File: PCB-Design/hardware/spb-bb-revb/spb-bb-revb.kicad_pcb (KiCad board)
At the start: 4 copper layers, 89.5 x 80 mm, 236 parts, among them J1 DC+, J10 U.FL L2, J11 U.FL D2, J12 DC+, J13 DC-, J14 V_ISO,HS in: 1 +, 2 -, J15 V_ISO,LS in: 1 +, 2 -, J16 CTRL2: 1 12V 2 GND 3 PWM_H 4 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, J17 FAN 12V: 1 +12V, 2 GND, J18 U.FL H3, J19 U.FL L3, J2 DC-, J20 U.FL D3, J21 U.FL H4, J22 U.FL L4, J23 U.FL D4, J24 AC, J25 AC, J26 AC, J27 AC, J28 1:NTC 2:DC- (LS domain!), J3 V_ISO,HS in: 1 +, 2 -, J4 V_ISO,LS in: 1 +, 2 -, J5 CTRL1: 1 12V 2 GND 3 PWM_H 4 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, J6 U.FL H1, J7 U.FL L1, J8 U.FL D1, J9 U.FL H2, Q1 EPC2361, Q2 EPC2361, Q3 EPC2361, Q4 EPC2361, Q5 EPC2361, Q6 EPC2361, Q7 EPC2361, Q8 EPC2361, U1 2EDF7275K, U2 2EDF7275K

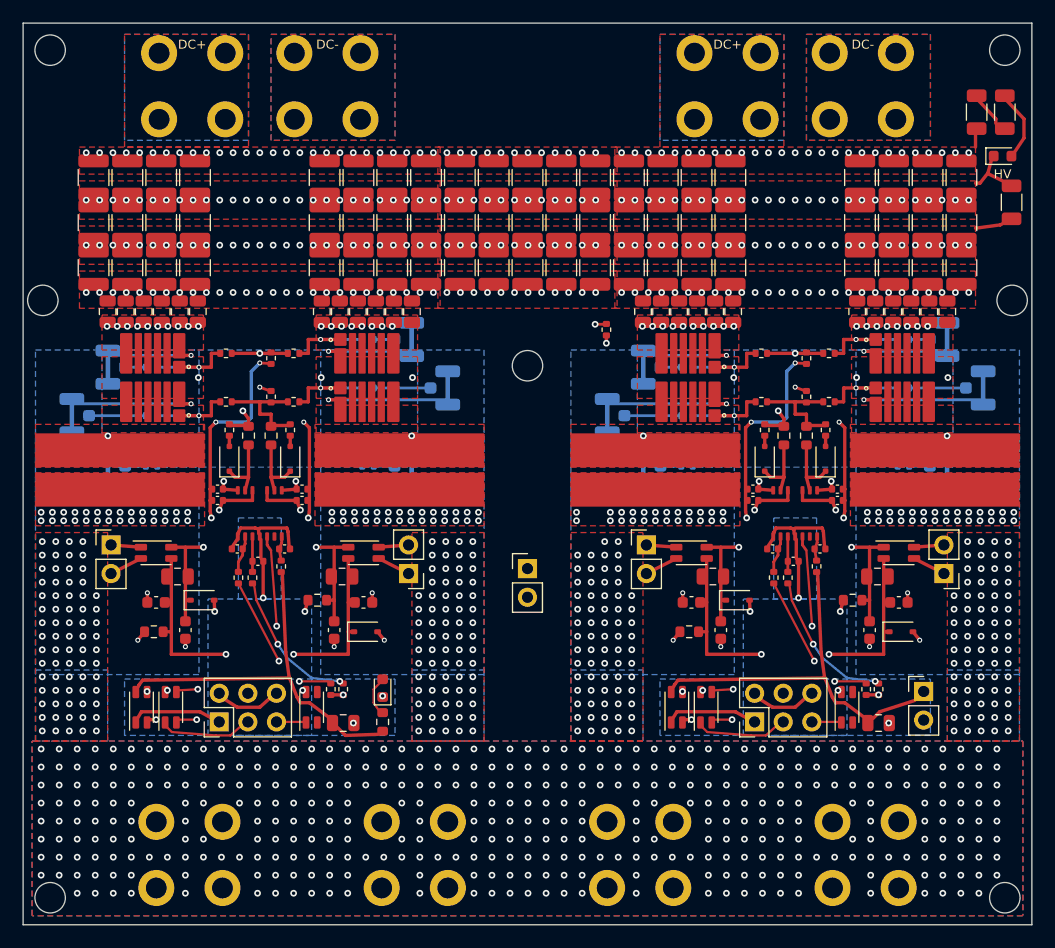
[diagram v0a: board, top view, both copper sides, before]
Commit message: ﻿Rev B as one leg: one DC pair, one AC bolt pad (option B drivers)
- make_kicad_bb_revb.py: one DC+/DC- REDCUBE pair at the centre feeding a laminated
  terminal row (L1/L3 DC+, L2/L4 DC-) over the full width; the four AC terminals replaced
  by one M6 bolt pad (AC_BOLT_M6, 14 mm pad, via rings); two drivers, one star per pair.
  231 parts, DRC 0/0/0, routing 0 failures
- schematic regenerated, check_sch_vs_pcb: 0 problems
- busbar: one DC pair per leg (6 bolt points), DRC clean
- Q3D export/post for the new terminals; leg Q3D setup at 2 % convergence
- deck: step 8 slides for the new layout (Q3D numbers follow)
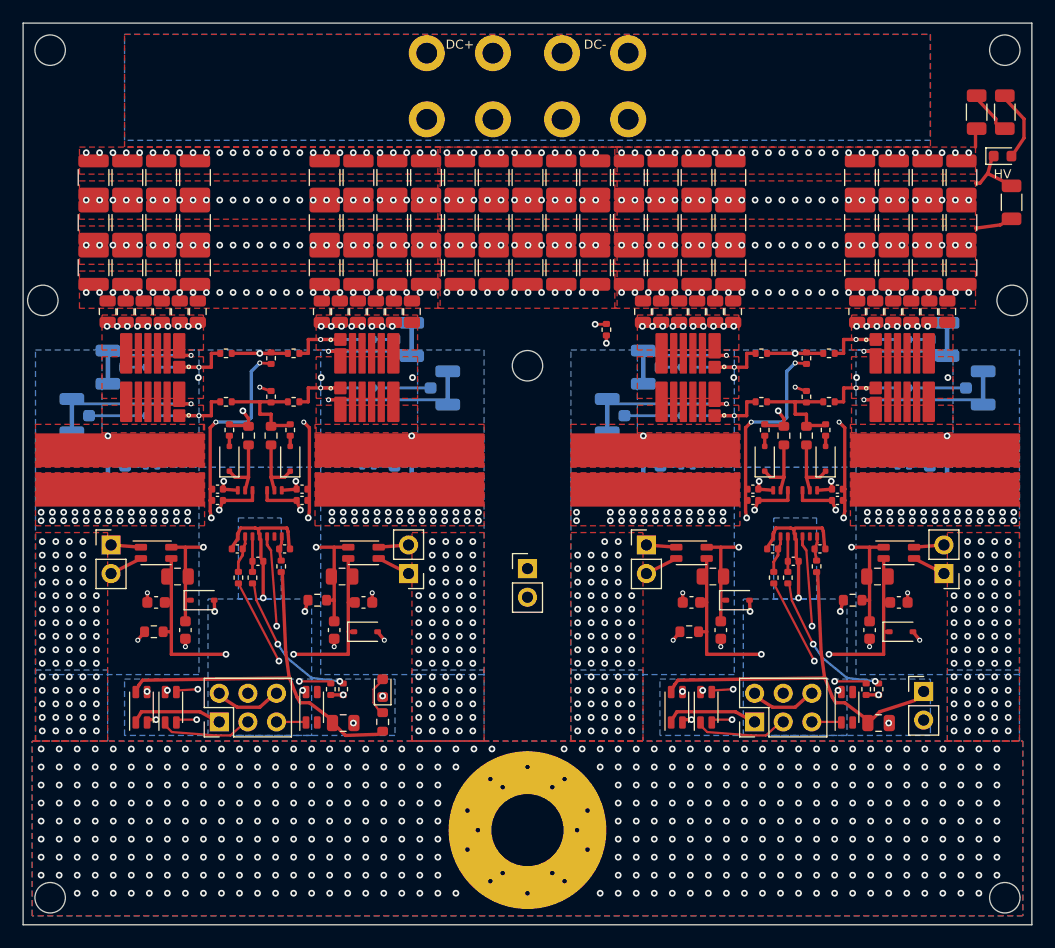
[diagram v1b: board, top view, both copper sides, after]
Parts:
- removed J24, J25, J26, J27: AC, TerminalBlock_Wuerth:Wuerth_REDCUBE-THR_WP-THRBU_74650174_THR
- removed J28: 1:NTC 2:DC- (LS domain!), Connector_PinHeader_2.54mm:PinHeader_1x02_P2.54mm_Vertical
- J12: value DC+ -> V_ISO,HS in: 1 +, 2 -; footprint TerminalBlock_Wuerth:Wuerth_REDCUBE-THR_WP-THRBU_74650174_THR -> Connector_PinHeader_2.54mm:PinHeader_1x02_P2.54mm_Vertical; moved to F.Cu
- J13: value DC- -> V_ISO,LS in: 1 +, 2 -; footprint TerminalBlock_Wuerth:Wuerth_REDCUBE-THR_WP-THRBU_74650174_THR -> Connector_PinHeader_2.54mm:PinHeader_1x02_P2.54mm_Vertical; moved to F.Cu
- J14: value V_ISO,HS in: 1 +, 2 - -> CTRL2: 1 12V 2 GND 3 PWM_H 4 PWM_L 5 DIS 6 GND; footprint Connector_PinHeader_2.54mm:PinHeader_1x02_P2.54mm_Vertical -> Connector_PinHeader_2.54mm:PinHeader_2x03_P2.54mm_Vertical
- J15: value V_ISO,LS in: 1 +, 2 - -> FAN 12V: 1 +12V, 2 GND
- J16: value CTRL2: 1 12V 2 GND 3 PWM_H 4 PWM_L 5 DIS 6 GND -> U.FL H3; footprint Connector_PinHeader_2.54mm:PinHeader_2x03_P2.54mm_Vertical -> spb_fab:U.FL_Hirose_U.FL-R-SMT-1_Vertical; moved to B.Cu
- J17: value FAN 12V: 1 +12V, 2 GND -> U.FL L3; footprint Connector_PinHeader_2.54mm:PinHeader_1x02_P2.54mm_Vertical -> spb_fab:U.FL_Hirose_U.FL-R-SMT-1_Vertical; moved to B.Cu
- J18: value U.FL H3 -> U.FL D3
- J19: value U.FL L3 -> U.FL H4
- J20: value U.FL D3 -> U.FL L4
- J21: value U.FL H4 -> U.FL D4
- J22: value U.FL L4 -> AC; footprint spb_fab:U.FL_Hirose_U.FL-R-SMT-1_Vertical -> spb_fab:AC_BOLT_M6; moved to F.Cu
- J23: value U.FL D4 -> 1:NTC 2:DC- (LS domain!); footprint spb_fab:U.FL_Hirose_U.FL-R-SMT-1_Vertical -> Connector_PinHeader_2.54mm:PinHeader_1x02_P2.54mm_Vertical; moved to F.Cu
- moved J22 56.0 mm to (150.0, 147.2)
- moved J13 43.8 mm to (186.9, 124.4), turned to 180 degrees
- moved J12 41.3 mm to (160.6, 121.9)
- moved J23 37.9 mm to (150.0, 124.0)
- moved J17 36.9 mm to (157.6, 110.4), turned to 180 degrees
- moved J16 32.8 mm to (160.8, 106.1), turned to 180 degrees
- moved J20 30.0 mm to (189.9, 108.0), turned to 0 degrees
- moved J19 30.0 mm to (186.8, 103.7), turned to 0 degrees
- moved J1 23.8 mm to (144.0, 81.2)
- moved J2 23.8 mm to (156.0, 81.2)
- moved J14 18.4 mm to (170.2, 137.6), turned to 90 degrees
- moved J21 11.2 mm to (186.8, 114.9)
- moved J15 10.6 mm to (185.2, 134.9), turned to 0 degrees
- moved J18 8.77 mm to (160.8, 114.9)
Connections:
- J12 pad 1: DCP -> VINA_P2
- J13 pad 1: DCN -> VINB_P2
- J14 pad 1: VINA_P2 -> C_12V2
- J14 pad 2: VINA_N2 -> C_GND2
- J15 pad 1: VINB_P2 -> +12V2
- J15 pad 2: VINB_N2 -> GNDI2
- J16 pad 1: C_12V2 -> UFL_H3
- J16 pad 2: C_GND2 -> KH2
- J17 pad 1: +12V2 -> UFL_L3
- J17 pad 2: GNDI2 -> KL2
- J18 pad 1: UFL_H3 -> UFL_D3
- J18 pad 2: KH2 -> LSRC3
- J19 pad 1: UFL_L3 -> UFL_H4
- J19 pad 2: KL2 -> KH2
- J20 pad 1: UFL_D3 -> UFL_L4
- J20 pad 2: LSRC3 -> KL2
- J21 pad 1: UFL_H4 -> UFL_D4
- J21 pad 2: KH2 -> LSRC4
- J22 pad 1: UFL_L4 -> SW
- J23 pad 1: UFL_D4 -> NTC
- J23 pad 2: LSRC4 -> DCN
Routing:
- net SW: vias 681 -> 700
- removed copper zone on In2.Cu, net DCN
- removed copper zone on B.Cu, net DCP
- removed copper zone on In1.Cu, net DCP
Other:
- board text added: "AC OUT: M6 bolt pad, 12 x 5 mm Cu bar bolted on, through the LEM HO 250-S to the load"
- board text removed: "AC OUT: 12 x 5 mm Cu bar across the four terminals, stub through LEM HO 250-S to the load"

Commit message: ﻿Rev B: one continuous capacitor bank on a uniform 3 mm grid
The per-block bank left an empty column at each block centre (Rev A DC entry). The bank is
now placed once for the leg: 3 rows x 25 x 10 uF 1210 at x = -36 ... +36 mm, no gaps
(75 bank + 24 bypass MLCCs). DRC 0/0/0, schematic = PCB (0 problems).
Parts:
- added C116: 10uF 100V X7S, spb_fab:C_1210_3225Metric_TightCrtYd, F.Cu at (153.0, 97.3)
- added C117: 10uF 100V X7S, spb_fab:C_1210_3225Metric_TightCrtYd, F.Cu at (156.0, 97.3)
- added C118: 10uF 100V X7S, spb_fab:C_1210_3225Metric_TightCrtYd, F.Cu at (159.0, 97.3)
- added C119: 10uF 100V X7S, spb_fab:C_1210_3225Metric_TightCrtYd, F.Cu at (162.0, 97.3)
- added C120: 10uF 100V X7S, spb_fab:C_1210_3225Metric_TightCrtYd, F.Cu at (165.0, 97.3)
- added C121: 10uF 100V X7S, spb_fab:C_1210_3225Metric_TightCrtYd, F.Cu at (168.0, 97.3)
- added C122: 10uF 100V X7S, spb_fab:C_1210_3225Metric_TightCrtYd, F.Cu at (171.0, 97.3)
- added C123: 10uF 100V X7S, spb_fab:C_1210_3225Metric_TightCrtYd, F.Cu at (174.0, 97.3)
- added C124: 10uF 100V X7S, spb_fab:C_1210_3225Metric_TightCrtYd, F.Cu at (177.0, 97.3)
- added C125: 10uF 100V X7S, spb_fab:C_1210_3225Metric_TightCrtYd, F.Cu at (180.0, 97.3)
- added C126: 10uF 100V X7S, spb_fab:C_1210_3225Metric_TightCrtYd, F.Cu at (183.0, 97.3)
- added C127: 10uF 100V X7S, spb_fab:C_1210_3225Metric_TightCrtYd, F.Cu at (186.0, 97.3)
- C100: value 4.7uF 25V X7R 0805 (12 V) -> 10uF 100V X7S; footprint Capacitor_SMD:C_0805_2012Metric -> spb_fab:C_1210_3225Metric_TightCrtYd
- C13, C14, C15, C16: value 10uF 100V X7S -> 1uF 16V X7R 0402; footprint spb_fab:C_1210_3225Metric_TightCrtYd -> Capacitor_SMD:C_0402_1005Metric
- C17, C18: value 10uF 100V X7S -> 100pF C0G 0402; footprint spb_fab:C_1210_3225Metric_TightCrtYd -> Capacitor_SMD:C_0402_1005Metric
- C19: value 10uF 100V X7S -> 22nF 25V X7R 0402; footprint spb_fab:C_1210_3225Metric_TightCrtYd -> Capacitor_SMD:C_0402_1005Metric
- C20, C23: value 10uF 100V X7S -> 4.7uF 25V X7R 0805; footprint spb_fab:C_1210_3225Metric_TightCrtYd -> Capacitor_SMD:C_0805_2012Metric
- C21, C22, C24, C25: value 10uF 100V X7S -> 4.7uF 16V X5R 0603; footprint spb_fab:C_1210_3225Metric_TightCrtYd -> Capacitor_SMD:C_0603_1608Metric
- C26: value 10uF 100V X7S -> 4.7uF 25V X7R 0805 (12 V); footprint spb_fab:C_1210_3225Metric_TightCrtYd -> Capacitor_SMD:C_0805_2012Metric
- C27, C28, C29, C30, C31, C32, C33, C34, C35, C36: value 10uF 100V X7S -> 1uF 100V X7S; footprint spb_fab:C_1210_3225Metric_TightCrtYd -> spb_fab:C_0805_2012Metric_TightCrtYd
- C37, C38: value 1uF 16V X7R 0402 -> 1uF 100V X7S; footprint Capacitor_SMD:C_0402_1005Metric -> spb_fab:C_0805_2012Metric_TightCrtYd
- C41, C42: value 100pF C0G 0402 -> 1uF 16V X7R 0402
- C43: value 22nF 25V X7R 0402 -> 100pF C0G 0402
- C44: value 4.7uF 25V X7R 0805 -> 100pF C0G 0402; footprint Capacitor_SMD:C_0805_2012Metric -> Capacitor_SMD:C_0402_1005Metric
- C45: value 4.7uF 16V X5R 0603 -> 22nF 25V X7R 0402; footprint Capacitor_SMD:C_0603_1608Metric -> Capacitor_SMD:C_0402_1005Metric
- C46, C49: value 4.7uF 16V X5R 0603 -> 4.7uF 25V X7R 0805; footprint Capacitor_SMD:C_0603_1608Metric -> Capacitor_SMD:C_0805_2012Metric
- C47: value 4.7uF 25V X7R 0805 -> 4.7uF 16V X5R 0603; footprint Capacitor_SMD:C_0805_2012Metric -> Capacitor_SMD:C_0603_1608Metric
- C50: value 4.7uF 25V X7R 0805 (12 V) -> 4.7uF 16V X5R 0603; footprint Capacitor_SMD:C_0805_2012Metric -> Capacitor_SMD:C_0603_1608Metric
- C51: value 1uF 100V X7S -> 4.7uF 16V X5R 0603; footprint spb_fab:C_0805_2012Metric_TightCrtYd -> Capacitor_SMD:C_0603_1608Metric
- C52: value 1uF 100V X7S -> 4.7uF 25V X7R 0805 (12 V); footprint spb_fab:C_0805_2012Metric_TightCrtYd -> Capacitor_SMD:C_0805_2012Metric
- C53, C54, C55, C56, C57, C58, C59, C60, C61, C62: value 1uF 100V X7S -> 10uF 100V X7S; footprint spb_fab:C_0805_2012Metric_TightCrtYd -> spb_fab:C_1210_3225Metric_TightCrtYd
- C87, C88, C89, C90: value 1uF 16V X7R 0402 -> 10uF 100V X7S; footprint Capacitor_SMD:C_0402_1005Metric -> spb_fab:C_1210_3225Metric_TightCrtYd
- C91, C92: value 100pF C0G 0402 -> 10uF 100V X7S; footprint Capacitor_SMD:C_0402_1005Metric -> spb_fab:C_1210_3225Metric_TightCrtYd
- C93: value 22nF 25V X7R 0402 -> 10uF 100V X7S; footprint Capacitor_SMD:C_0402_1005Metric -> spb_fab:C_1210_3225Metric_TightCrtYd
- C94, C97: value 4.7uF 25V X7R 0805 -> 10uF 100V X7S; footprint Capacitor_SMD:C_0805_2012Metric -> spb_fab:C_1210_3225Metric_TightCrtYd
- C95, C96, C98, C99: value 4.7uF 16V X5R 0603 -> 10uF 100V X7S; footprint Capacitor_SMD:C_0603_1608Metric -> spb_fab:C_1210_3225Metric_TightCrtYd
- moved C78 74.5 mm to (114.0, 93.3)
- moved C38 66.9 mm to (187.2, 101.2), turned to 90 degrees
- moved C37 65.1 mm to (185.7, 101.2), turned to 90 degrees
- moved C32 56.9 mm to (168.2, 101.2)
- moved C45 56.8 mm to (175.9, 122.2), turned to 0 degrees
- moved C44 54.6 mm to (173.6, 123.3)
- moved C57 54.6 mm to (126.0, 89.3)
- moved C41 53.5 mm to (177.5, 117.0)
- moved C58 53.2 mm to (129.0, 89.3)
- moved C31 52.3 mm to (166.6, 101.2)
- moved C59 51.8 mm to (132.0, 89.3)
- moved C42 51.7 mm to (177.5, 118.0)
- moved C79 51.2 mm to (117.0, 93.3)
- moved C53 50.9 mm to (114.0, 89.3)
- moved C83 50.7 mm to (129.0, 93.3)
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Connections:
- C100 pad 1: +12V2 -> DCP
- C100 pad 2: GNDI2 -> DCN
- C101 pad 1: DCN -> DCP
- C101 pad 2: DCP -> DCN
- C102 pad 1: DCN -> DCP
- C102 pad 2: DCP -> DCN
- C106 pad 1: DCP -> DCN
- C106 pad 2: DCN -> DCP
- C107 pad 1: DCP -> DCN
- C107 pad 2: DCN -> DCP
- C108 pad 1: DCP -> DCN
- C108 pad 2: DCN -> DCP
- C109 pad 1: DCP -> DCN
- C109 pad 2: DCN -> DCP
- C110 pad 1: DCP -> DCN
- C110 pad 2: DCN -> DCP
- C13 pad 1: DCN -> KH1
- C13 pad 2: DCP -> VDDA1
- C14 pad 1: DCN -> KH1
- C14 pad 2: DCP -> VEEA1
- C15 pad 1: DCN -> VEEB1
- C15 pad 2: DCP -> KL1
- C16 pad 1: DCN -> VDDB1
- C16 pad 2: DCP -> KL1
- C17 pad 1: DCN -> GNDI1
- C17 pad 2: DCP -> INA1
- C18 pad 1: DCN -> INB1
- C18 pad 2: DCP -> GNDI1
- C19 pad 1: DCN -> VDDI1
- C19 pad 2: DCP -> GNDI1
- C20 pad 1: DCN -> VEEA1
- C20 pad 2: DCP -> VDDA1
- C21 pad 1: DCP -> KH1
- C21 pad 2: DCN -> VDDA1
- C22 pad 1: DCP -> KH1
- C22 pad 2: DCN -> VEEA1
- C23 pad 1: DCP -> VEEB1
- C23 pad 2: DCN -> VDDB1
- C24 pad 1: DCP -> KL1
- C24 pad 2: DCN -> VEEB1
- C25 pad 1: DCP -> VDDB1
- C25 pad 2: DCN -> KL1
- C26 pad 1: DCP -> +12V1
- C26 pad 2: DCN -> GNDI1
- C29 pad 1: DCN -> DCP
- C29 pad 2: DCP -> DCN
- C30 pad 1: DCN -> DCP
- C30 pad 2: DCP -> DCN
- C31 pad 1: DCN -> DCP
- C31 pad 2: DCP -> DCN
- C32 pad 1: DCN -> DCP
- C32 pad 2: DCP -> DCN
- C33 pad 1: DCN -> DCP
- C33 pad 2: DCP -> DCN
- C34 pad 1: DCN -> DCP
- C34 pad 2: DCP -> DCN
- C35 pad 1: DCN -> DCP
- C35 pad 2: DCP -> DCN
- C36 pad 1: DCN -> DCP
- C36 pad 2: DCP -> DCN
- C37 pad 1: KH1 -> DCP
- C37 pad 2: VDDA1 -> DCN
- C38 pad 1: KH1 -> DCP
- C38 pad 2: VEEA1 -> DCN
- C39 pad 1: VEEB1 -> KH2
- C39 pad 2: KL1 -> VDDA2
- C40 pad 1: VDDB1 -> KH2
- C40 pad 2: KL1 -> VEEA2
- C41 pad 1: GNDI1 -> VEEB2
- C41 pad 2: INA1 -> KL2
- C42 pad 1: INB1 -> VDDB2
- C42 pad 2: GNDI1 -> KL2
- C43 pad 1: VDDI1 -> GNDI2
- C43 pad 2: GNDI1 -> INA2
- C44 pad 1: VEEA1 -> INB2
- C44 pad 2: VDDA1 -> GNDI2
- C45 pad 1: KH1 -> VDDI2
- C45 pad 2: VDDA1 -> GNDI2
- C46 pad 1: KH1 -> VEEA2
- C46 pad 2: VEEA1 -> VDDA2
- C47 pad 1: VEEB1 -> KH2
- C47 pad 2: VDDB1 -> VDDA2
- C48 pad 1: KL1 -> KH2
- C48 pad 2: VEEB1 -> VEEA2
- C49 pad 1: VDDB1 -> VEEB2
- C49 pad 2: KL1 -> VDDB2
- C50 pad 1: +12V1 -> KL2
- C50 pad 2: GNDI1 -> VEEB2
- C51 pad 1: DCP -> VDDB2
- C51 pad 2: DCN -> KL2
- C52 pad 1: DCP -> +12V2
- C52 pad 2: DCN -> GNDI2
- C53 pad 1: DCP -> DCN
- C53 pad 2: DCN -> DCP
- C54 pad 1: DCP -> DCN
- C54 pad 2: DCN -> DCP
- C55 pad 1: DCP -> DCN
- C55 pad 2: DCN -> DCP
- C56 pad 1: DCP -> DCN
- C56 pad 2: DCN -> DCP
- C57 pad 1: DCP -> DCN
- C57 pad 2: DCN -> DCP
- C58 pad 1: DCP -> DCN
- C58 pad 2: DCN -> DCP
- C59 pad 1: DCP -> DCN
- C59 pad 2: DCN -> DCP
- C60 pad 1: DCP -> DCN
- C60 pad 2: DCN -> DCP
- C61 pad 1: DCP -> DCN
- C61 pad 2: DCN -> DCP
- C62 pad 1: DCP -> DCN
- C62 pad 2: DCN -> DCP
- C71 pad 1: DCP -> DCN
- C71 pad 2: DCN -> DCP
- C72 pad 1: DCP -> DCN
- C72 pad 2: DCN -> DCP
- C73 pad 1: DCP -> DCN
- C73 pad 2: DCN -> DCP
- C74 pad 1: DCP -> DCN
- C74 pad 2: DCN -> DCP
- C75 pad 1: DCP -> DCN
- C75 pad 2: DCN -> DCP
- C76 pad 1: DCP -> DCN
- C76 pad 2: DCN -> DCP
- C77 pad 1: DCP -> DCN
- C77 pad 2: DCN -> DCP
- C79 pad 1: DCN -> DCP
- C79 pad 2: DCP -> DCN
- C80 pad 1: DCN -> DCP
- C80 pad 2: DCP -> DCN
- C81 pad 1: DCN -> DCP
- C81 pad 2: DCP -> DCN
- C82 pad 1: DCN -> DCP
- C82 pad 2: DCP -> DCN
- C83 pad 1: DCN -> DCP
- C83 pad 2: DCP -> DCN
- C84 pad 1: DCN -> DCP
- C84 pad 2: DCP -> DCN
- C85 pad 1: DCN -> DCP
- C85 pad 2: DCP -> DCN
- C86 pad 1: DCN -> DCP
- C86 pad 2: DCP -> DCN
- C87 pad 1: KH2 -> DCP
- C87 pad 2: VDDA2 -> DCN
- C88 pad 1: KH2 -> DCP
- C88 pad 2: VEEA2 -> DCN
- C89 pad 1: VEEB2 -> DCP
- C89 pad 2: KL2 -> DCN
- C90 pad 1: VDDB2 -> DCP
- C90 pad 2: KL2 -> DCN
- C91 pad 1: GNDI2 -> DCP
- C91 pad 2: INA2 -> DCN
- C92 pad 1: INB2 -> DCP
- C92 pad 2: GNDI2 -> DCN
- C93 pad 1: VDDI2 -> DCP
- C93 pad 2: GNDI2 -> DCN
- C94 pad 1: VEEA2 -> DCP
- C94 pad 2: VDDA2 -> DCN
- C95 pad 1: KH2 -> DCP
- C95 pad 2: VDDA2 -> DCN
- C96 pad 1: KH2 -> DCP
- C96 pad 2: VEEA2 -> DCN
- C97 pad 1: VEEB2 -> DCP
- C97 pad 2: VDDB2 -> DCN
- C98 pad 1: KL2 -> DCP
- C98 pad 2: VEEB2 -> DCN
- C99 pad 1: VDDB2 -> DCP
- C99 pad 2: KL2 -> DCN

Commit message: ﻿Rev B: TDK 22 uF 2220 bank (3 % ripple) and 10 bypass caps per cell
- bank: 20 x TDK C5750X7S2A226M280KB in two rows on new strips (row B 12 next to the
  cells, row A 8 clear of the DC terminal pins): 127 uF effective per leg at 75 V,
  2.9 % ripple at 50 kHz with the three legs of a level sharing the bus
- bypass: 6 x 0805 1 uF on top (loop unchanged) + 4 on the bottom per cell (L4 islands on
  the existing through vias), mirrored positions so all four cells are identical
- bb_geometry.build() accepts row overrides (Rev A unchanged)
- DRC 0/0/0, schematic = PCB (0 problems); Q3D export with bottom bypass groups;
  post-processing with the measured C at 75 V; deck: sizing, selection, bypass slides
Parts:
- removed C100, C101, C102, C103, C104, C105, C106, C107, C108, C109, C110, C111, C112, C113, C114, C115, C116, C117, C118, C119, C120, C121, C122, C123, C124, C125, C126, C127, C89, C90, C91, C92, C93, C94, C95, C96, C97, C98, C99: 10uF 100V X7S, spb_fab:C_1210_3225Metric_TightCrtYd
- C27, C28, C29, C30, C31, C32, C33, C34: moved to B.Cu
- C39, C40, C41, C42: value 1uF 16V X7R 0402 -> 1uF 100V X7S; footprint Capacitor_SMD:C_0402_1005Metric -> spb_fab:C_0805_2012Metric_TightCrtYd
- C43, C44: value 100pF C0G 0402 -> 1uF 100V X7S; footprint Capacitor_SMD:C_0402_1005Metric -> spb_fab:C_0805_2012Metric_TightCrtYd
- C45: value 22nF 25V X7R 0402 -> 1uF 100V X7S; footprint Capacitor_SMD:C_0402_1005Metric -> spb_fab:C_0805_2012Metric_TightCrtYd
- C46: value 4.7uF 25V X7R 0805 -> 1uF 100V X7S; footprint Capacitor_SMD:C_0805_2012Metric -> spb_fab:C_0805_2012Metric_TightCrtYd
- C47, C48, C50: value 4.7uF 16V X5R 0603 -> 1uF 16V X7R 0402; footprint Capacitor_SMD:C_0603_1608Metric -> Capacitor_SMD:C_0402_1005Metric
- C49: value 4.7uF 25V X7R 0805 -> 1uF 16V X7R 0402; footprint Capacitor_SMD:C_0805_2012Metric -> Capacitor_SMD:C_0402_1005Metric
- C51: value 4.7uF 16V X5R 0603 -> 100pF C0G 0402; footprint Capacitor_SMD:C_0603_1608Metric -> Capacitor_SMD:C_0402_1005Metric
- C52: value 4.7uF 25V X7R 0805 (12 V) -> 100pF C0G 0402; footprint Capacitor_SMD:C_0805_2012Metric -> Capacitor_SMD:C_0402_1005Metric
- C53: value 10uF 100V X7S -> 22nF 25V X7R 0402; footprint spb_fab:C_1210_3225Metric_TightCrtYd -> Capacitor_SMD:C_0402_1005Metric
- C54, C57: value 10uF 100V X7S -> 4.7uF 25V X7R 0805; footprint spb_fab:C_1210_3225Metric_TightCrtYd -> Capacitor_SMD:C_0805_2012Metric
- C55, C56, C58, C59: value 10uF 100V X7S -> 4.7uF 16V X5R 0603; footprint spb_fab:C_1210_3225Metric_TightCrtYd -> Capacitor_SMD:C_0603_1608Metric
- C60: value 10uF 100V X7S -> 4.7uF 25V X7R 0805 (12 V); footprint spb_fab:C_1210_3225Metric_TightCrtYd -> Capacitor_SMD:C_0805_2012Metric
- C61, C62, C63, C64, C65, C66, C67, C68: value 10uF 100V X7S -> 1uF 100V X7S; footprint spb_fab:C_1210_3225Metric_TightCrtYd -> spb_fab:C_0805_2012Metric_TightCrtYd; moved to B.Cu
- C69, C70, C71, C72, C73, C74, C75, C76, C77, C78, C79, C80, C81, C82, C83, C84, C85, C86, C87, C88: value 10uF 100V X7S -> 22uF 100V X7S 2220; footprint spb_fab:C_1210_3225Metric_TightCrtYd -> spb_fab:C_2220_5750Metric_TightCrtYd
- moved C53 70.2 mm to (175.9, 122.2), turned to 0 degrees
- moved C60 66.9 mm to (181.2, 137.7), turned to 0 degrees
- moved C57 65.4 mm to (181.1, 124.7), turned to 0 degrees
- moved C58 65.2 mm to (180.3, 129.4)
- moved C59 63.4 mm to (182.9, 127.0), turned to 0 degrees
- moved C75 63.0 mm to (117.0, 88.3)
- moved C55 61.9 mm to (167.2, 129.4)
- moved C54 60.8 mm to (166.4, 124.7), turned to 0 degrees
- moved C56 56.1 mm to (164.6, 127.0), turned to 0 degrees
- moved C73 51.0 mm to (123.0, 88.3)
- moved C34 49.1 mm to (131.8, 101.2), turned to -90 degrees
- moved C33 45.9 mm to (133.4, 101.2), turned to -90 degrees
- moved C30 44.3 mm to (120.8, 101.2), turned to -90 degrees
- moved C27 44.3 mm to (116.0, 101.2), turned to -90 degrees
- moved C28 44.3 mm to (117.5, 101.2), turned to -90 degrees
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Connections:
- C27 pad 1: DCP -> DCN
- C27 pad 2: DCN -> DCP
- C28 pad 1: DCP -> DCN
- C28 pad 2: DCN -> DCP
- C29 pad 1: DCP -> DCN
- C29 pad 2: DCN -> DCP
- C30 pad 1: DCP -> DCN
- C30 pad 2: DCN -> DCP
- C31 pad 1: DCP -> DCN
- C31 pad 2: DCN -> DCP
- C32 pad 1: DCP -> DCN
- C32 pad 2: DCN -> DCP
- C33 pad 1: DCP -> DCN
- C33 pad 2: DCN -> DCP
- C34 pad 1: DCP -> DCN
- C34 pad 2: DCN -> DCP
- C39 pad 1: KH2 -> DCP
- C39 pad 2: VDDA2 -> DCN
- C40 pad 1: KH2 -> DCP
- C40 pad 2: VEEA2 -> DCN
- C41 pad 1: VEEB2 -> DCP
- C41 pad 2: KL2 -> DCN
- C42 pad 1: VDDB2 -> DCP
- C42 pad 2: KL2 -> DCN
- C43 pad 1: GNDI2 -> DCP
- C43 pad 2: INA2 -> DCN
- C44 pad 1: INB2 -> DCP
- C44 pad 2: GNDI2 -> DCN
- C45 pad 1: VDDI2 -> DCP
- C45 pad 2: GNDI2 -> DCN
- C46 pad 1: VEEA2 -> DCP
- C46 pad 2: VDDA2 -> DCN
- C49 pad 2: VDDB2 -> KL2
- C50 pad 1: KL2 -> VDDB2
- C50 pad 2: VEEB2 -> KL2
- C51 pad 1: VDDB2 -> GNDI2
- C51 pad 2: KL2 -> INA2
- C52 pad 1: +12V2 -> INB2
- C53 pad 1: DCN -> VDDI2
- C53 pad 2: DCP -> GNDI2
- C54 pad 1: DCN -> VEEA2
- C54 pad 2: DCP -> VDDA2
- C55 pad 1: DCN -> KH2
- C55 pad 2: DCP -> VDDA2
- C56 pad 1: DCN -> KH2
- C56 pad 2: DCP -> VEEA2
- C57 pad 1: DCN -> VEEB2
- C57 pad 2: DCP -> VDDB2
- C58 pad 1: DCN -> KL2
- C58 pad 2: DCP -> VEEB2
- C59 pad 1: DCN -> VDDB2
- C59 pad 2: DCP -> KL2
- C60 pad 1: DCN -> +12V2
- C60 pad 2: DCP -> GNDI2
- C78 pad 1: DCP -> DCN
- C78 pad 2: DCN -> DCP
- C79 pad 1: DCP -> DCN
- C79 pad 2: DCN -> DCP
- C80 pad 1: DCP -> DCN
- C80 pad 2: DCN -> DCP
- C81 pad 1: DCP -> DCN
- C81 pad 2: DCN -> DCP
- C82 pad 1: DCP -> DCN
- C82 pad 2: DCN -> DCP
- C83 pad 1: DCP -> DCN
- C83 pad 2: DCN -> DCP
- C84 pad 1: DCP -> DCN
- C84 pad 2: DCN -> DCP
- C85 pad 1: DCP -> DCN
- C85 pad 2: DCN -> DCP
- C86 pad 1: DCP -> DCN
- C86 pad 2: DCN -> DCP
- C87 pad 1: DCP -> DCN
- C87 pad 2: DCN -> DCP
- C88 pad 1: DCP -> DCN
- C88 pad 2: DCN -> DCP
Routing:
- net DCP: track 3.64 -> 2.40 mm
- added copper zone on B.Cu, net DCP

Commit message: ﻿Symmetric cells: mirror-pair via pruning, Kelvin collectors on L4, vias in the shunt pad
- the left/right loop difference (0.13-0.15 nH) came from power vias that survived the
  clearance pruning in one cell and not in its mirror (2 source-row DC- vias only in the
  right cells); power vias are now pruned in mirror pairs about the block centre
- Kelvin collectors moved from L2 (DC- return plane) to L4; return vias inside the shunt
  SHLD pad in the main board
- no-shunt assembly: 0.405 / 0.405 / 0.406 / 0.410 nH (was 0.56 / 0.41 / 0.55 / 0.41)
- study variants noshunt_rot0, model checks (sink cell, mirrored geometry) in the loop model
- reports/shunt-loop/figs/cell_symmetry.png (left vs right cell figure)
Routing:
- net KL2: vias 9 -> 11
- net SW: vias 700 -> 698
- net KL1: vias 9 -> 11
- net DCP: vias 168 -> 164
- net DCN: vias 241 -> 409

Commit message: Rev B: 3D models for every part, board STEP, design-flow deck with final loop results
- make_3d_models_revb.py: box models (STEP + VRML) for 2EDF7275K, PMK UFCS, TDK 2220 (2.8 mm),
  WE-CNSW 1206, M6 AC bolt + Cu bar, LAM 4 + spreader; parts with project models move to spb_fab
- board STEP export (fab/spb-bb-revb.step); DRC 0/0/0, schematic = PCB
- render_3d_revb.py: 3D views for the deck from the KiCad models
- deck (44 slides): Rev B bypass figure, 3D slides, fast-loop Q3D results (0.69 nH with shunt,
  0.41 nH without, cells symmetric), shunt study, symmetry cause/fix; old full-board/busbar Q3D marked
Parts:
- L1, L10, L2, L3, L4, L5, L6, L7, L8, L9: footprint Inductor_SMD:L_CommonMode_Wurth_WE-CNSW-1206 -> spb_fab:L_CommonMode_Wurth_WE-CNSW-1206
